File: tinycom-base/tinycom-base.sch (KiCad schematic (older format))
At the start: 9 parts, among them J1 MICRO_SD_HINGE, P1 CONN_02X08, P2 CONN_02X08, P3 USB_A, P4 CONN_01X12, P5 CONN_02X12, U1 OLIMEX_IC_AXP209, U2 STM32-48PIN, U3 fpc_24

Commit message: add base
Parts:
- removed P4: CONN_01X12, Pin_Headers:Pin_Header_Straight_1x12, symbol CONN_01X12
- removed P5: CONN_02X12, Pin_Headers:Pin_Header_Straight_2x12, symbol CONN_02X12
- removed U2: STM32-48PIN, mods:QFP50P900X900X160-48N, symbol STM32-48PIN
- removed U3: fpc_24, tinycom:fpc_24, symbol fpc_24
- added P4: USB_B, Connect:USB_Micro-B, symbol USB_B
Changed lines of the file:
@@
 LIBS:armory
 LIBS:stm32-48pin-devBoard
-LIBS:tinycom-pwm-cache
 EELAYER 25 0
 EELAYER END
@@
 $EndComp
 $Comp
-L CONN_02X12 P5
-U 1 1 562C6235
-P 4950 6400
-F 0 "P5" H 4950 7050 50  0000 C CNN
-F 1 "CONN_02X12" V 4950 6400 50  0000 C CNN
-F 2 "Pin_Headers:Pin_Header_Straight_2x12" H 4950 5200 60  0001 C CNN
-F 3 "" H 4950 5200 60  0000 C CNN
-	1    4950 6400
+L USB_B P4
+U 1 1 562CE6C3
+P 5200 6000
+F 0 "P4" H 5400 5800 50  0000 C CNN
+F 1 "USB_B" H 5150 6200 50  0000 C CNN
+F 2 "Connect:USB_Micro-B" V 5150 5900 60  0001 C CNN
+F 3 "" V 5150 5900 60  0000 C CNN
+	1    5200 6000
 	1    0    0    -1
 $EndComp
-$Comp
-L CONN_01X12 P4
-U 1 1 562C6348
-P 4450 6400
-F 0 "P4" H 4450 7050 50  0000 C CNN
-F 1 "CONN_01X12" V 4550 6400 50  0000 C CNN
-F 2 "Pin_Headers:Pin_Header_Straight_1x12" H 4450 6400 60  0001 C CNN
-F 3 "" H 4450 6400 60  0000 C CNN
-	1    4450 6400
-	1    0    0    -1
-$EndComp
-$Comp
-L STM32-48PIN U2
-U 1 1 562C67D9
-P 9350 2650
-F 0 "U2" H 8350 4400 60  0000 C CNN
-F 1 "STM32-48PIN" H 8600 850 60  0000 C CNN
-F 2 "mods:QFP50P900X900X160-48N" H 9350 2650 60  0001 C CNN
-F 3 "" H 9350 2650 60  0000 C CNN
-	1    9350 2650
-	1    0    0    -1
-$EndComp
-$Comp
-L fpc_24 U3
-U 1 1 562CDBDB
-P 9250 5050
-F 0 "U3" H 9250 5050 60  0000 C CNN
-F 1 "fpc_24" H 9250 5050 60  0000 C CNN
-F 2 "tinycom:fpc_24" H 9250 5050 60  0000 C CNN
-F 3 "" H 9250 5050 60  0000 C CNN
-	1    9250 5050
-	1    0    0    -1
-$EndComp

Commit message: xxx
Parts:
- U1: footprint ax209:ax209-OLIMEX_IC_QFN48 -> tinycom:ax209-OLIMEX_IC_QFN48
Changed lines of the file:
@@
 F 0 "U1" H 2350 6280 50  0000 L BNN
 F 1 "OLIMEX_IC_AXP209" H 2350 1250 50  0000 L BNN
-F 2 "ax209:ax209-OLIMEX_IC_QFN48" H 2850 4000 50  0001 C CNN
+F 2 "tinycom:ax209-OLIMEX_IC_QFN48" H 2850 4000 50  0001 C CNN
 F 3 "" H 2850 3850 60  0000 C CNN
 	1    2850 3850

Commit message: prepare base
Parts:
- removed U1: OLIMEX_IC_AXP209, tinycom:ax209-OLIMEX_IC_QFN48, symbol OLIMEX_IC_AXP209
- added C1, C10, C13, C2, C3, C4, C5, C6, C7, C8, C9: C_Small, Capacitors_SMD:C_0805, symbol C_Small
- added C11, C12: CP_Small, Capacitors_Elko_ThroughHole:Elko_vert_11.2x6.3mm_RM2.5_CopperClear, symbol CP_Small
- added D1: D_Schottky_Small, Diodes_SMD:SMA_Standard, symbol D_Schottky_Small
- added L1, L2, L3: SMD-INDUCTOR-2.2UH-20%-1.2A(0805), cd32:CD32, symbol SMD-INDUCTOR-2.2UH-20%-1.2A(0805)
- added R1, R10, R11, R12, R2, R3, R4, R5, R6, R7, R8, R9: R_Small, Resistors_SMD:R_0805, symbol R_Small
- added U1, U2, U3: SY8008BAAC, opendous:SOT23-5_Opendous, symbol SY8008BAAC
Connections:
- net UART1_TX: now reaches P1.1 (P1)
- net UDP1: now reaches P1.10 (P10)
- net UDP1: now also P3.3 (D+)
- net SDC0_CMD: now reaches P1.11 (P11)
- net SDC0_CMD: now also J1.3 (CMD), R10.2
- net UDM1: now reaches P1.12 (P12)
- net UDM1: now also P3.2 (D-)
- net SDC0_D3: now reaches P1.13 (P13)
- net SDC0_D3: now also J1.2 (CD/DAT3), R11.2
- net UDP0: now reaches P1.14 (P14)
- net UDP0: now also P4.3 (D+)
- net SDC0_D2: now reaches P1.15 (P15)
- net SDC0_D2: now also J1.1 (DAT2), R12.2
- net UDM0: now reaches P1.16 (P16)
- net UDM0: now also P4.2 (D-)
- net GND: now reaches P1.2 (P2)
- net GND: now also J1.10 (GND2), J1.11 (GND3), J1.12 (GND4), J1.6 (VSS), J1.9 (GND1), P2.2 (P2), P3.4 (GND), P4.4 (GND), P4.5 (shield), C1.2, C10.1, C11.2, C12.2, C13.1, C2.1, C3.2, C4.2, C5.1, C6.1, C7.1, C8.1, C9.1, R2.2, R4.2, R6.2, R7.2, U1.2 (GND), U2.2 (GND), U3.2 (GND)
- net UART1_RX: now reaches P1.3 (P3)
- net VCC_15: now reaches P1.4 (P4)
- net VCC_15: now also C5.2, L3.2, R3.1
- net SDC0_D1: now reaches P1.5 (P5)
- net SDC0_D1: now also J1.8 (DAT1), R8.2
- net VCC_14: now reaches P1.6 (P6)
- net VCC_14: now also C6.2, L2.2, R5.1
- net SDC0_D0: now reaches P1.7 (P7)
- net SDC0_D0: now also J1.7 (DAT0), R9.2
- net +3V3: now reaches P1.8 (P8)
- net +3V3: now also J1.4 (VDD), C13.2, C2.2, C8.2, D1.2 (A), L1.2, R1.1, R10.1, R11.1, R12.1, R8.1, R9.1
- net SDC0_CLK: now reaches P1.9 (P9)
- net SDC0_CLK: now also J1.5 (CLK)
- net VCC_30: now reaches P2.4 (P4)
- net VCC_30: now also C7.2, D1.1 (K), R7.1
- net +5V: now reaches P3.1 (VCC)
- net +5V: now also P4.1 (VCC), C1.1, C10.2, C11.1, C12.1, C3.1, C4.1, C9.2, U1.1 (EN), U1.4 (IN), U2.1 (EN), U2.4 (IN), U3.1 (EN), U3.4 (IN)
- new net: L1.1, U1.3 (LX)
- new net: R1.2, R2.1, U1.5 (FB)
- new net: L2.1, U2.3 (LX)
- new net: R5.2, R6.1, U2.5 (FB)
- new net: L3.1, U3.3 (LX)
- new net: R3.2, R4.1, U3.5 (FB)
- no-connect marks 0 -> 1
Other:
- moved on the sheet: J1, P1, P2, P3, P4

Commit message: adjust base
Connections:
- net GND: no longer P4.5 (shield)
- net UART1_RX: no longer names the net of P1.3 (P3)
- net UART1_TX: no longer names the net of P1.1 (P1)
- no-connect marks 1 -> 18
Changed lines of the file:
@@
 $EndComp
 $Comp
-L +5V #PWR14
+L +5V #PWR01
 U 1 1 562DA8F7
 P 5250 4200
-F 0 "#PWR14" H 5250 4050 50  0001 C CNN
+F 0 "#PWR01" H 5250 4050 50  0001 C CNN
 F 1 "+5V" H 5250 4340 50  0000 C CNN
 F 2 "" H 5250 4200 60  0000 C CNN
@@
 $EndComp
 $Comp
-L GND #PWR15
+L GND #PWR02
 U 1 1 562DA928
 P 5250 4600
-F 0 "#PWR15" H 5250 4350 50  0001 C CNN
+F 0 "#PWR02" H 5250 4350 50  0001 C CNN
 F 1 "GND" H 5250 4450 50  0000 C CNN
 F 2 "" H 5250 4600 60  0000 C CNN
@@
 UDP0
 $Comp
-L +5V #PWR16
+L +5V #PWR03
 U 1 1 562DAC42
 P 5300 5050
-F 0 "#PWR16" H 5300 4900 50  0001 C CNN
+F 0 "#PWR03" H 5300 4900 50  0001 C CNN
 F 1 "+5V" H 5300 5190 50  0000 C CNN
 F 2 "" H 5300 5050 60  0000 C CNN
@@
 $EndComp
 $Comp
-L GND #PWR17
+L GND #PWR04
 U 1 1 562DAC77
 P 5300 5500
-F 0 "#PWR17" H 5300 5250 50  0001 C CNN
+F 0 "#PWR04" H 5300 5250 50  0001 C CNN
 F 1 "GND" H 5300 5350 50  0000 C CNN
 F 2 "" H 5300 5500 60  0000 C CNN
@@
 UDP1
 $Comp
-L GND #PWR5
+L GND #PWR05
 U 1 1 562DAF0B
 P 1350 1750
-F 0 "#PWR5" H 1350 1500 50  0001 C CNN
+F 0 "#PWR05" H 1350 1500 50  0001 C CNN
 F 1 "GND" H 1350 1600 50  0000 C CNN
 F 2 "" H 1350 1750 60  0000 C CNN
@@
 $EndComp
 $Comp
-L +5V #PWR3
+L +5V #PWR06
 U 1 1 562DAF87
 P 1250 1350
-F 0 "#PWR3" H 1250 1200 50  0001 C CNN
+F 0 "#PWR06" H 1250 1200 50  0001 C CNN
 F 1 "+5V" H 1250 1490 50  0000 C CNN
 F 2 "" H 1250 1350 60  0000 C CNN
@@
 $EndComp
 $Comp
-L +5V #PWR1
+L +5V #PWR07
 U 1 1 562DB0A5
 P 1150 2550
-F 0 "#PWR1" H 1150 2400 50  0001 C CNN
+F 0 "#PWR07" H 1150 2400 50  0001 C CNN
 F 1 "+5V" H 1150 2690 50  0000 C CNN
 F 2 "" H 1150 2550 60  0000 C CNN
@@
 $EndComp
 $Comp
-L GND #PWR6
+L GND #PWR08
 U 1 1 562DB1B7
 P 1350 2900
-F 0 "#PWR6" H 1350 2650 50  0001 C CNN
+F 0 "#PWR08" H 1350 2650 50  0001 C CNN
 F 1 "GND" H 1350 2750 50  0000 C CNN
 F 2 "" H 1350 2900 60  0000 C CNN
@@
 $EndComp
 $Comp
-L +5V #PWR2
+L +5V #PWR09
 U 1 1 562DB2B7
 P 1150 3800
-F 0 "#PWR2" H 1150 3650 50  0001 C CNN
+F 0 "#PWR09" H 1150 3650 50  0001 C CNN
 F 1 "+5V" H 1150 3940 50  0000 C CNN
 F 2 "" H 1150 3800 60  0000 C CNN
@@
 $EndComp
 $Comp
-L GND #PWR4
+L GND #PWR010
 U 1 1 562DB346
 P 1300 4150
-F 0 "#PWR4" H 1300 3900 50  0001 C CNN
+F 0 "#PWR010" H 1300 3900 50  0001 C CNN
 F 1 "GND" H 1300 4000 50  0000 C CNN
 F 2 "" H 1300 4150 60  0000 C CNN
@@
 VCC_15
 $Comp
-L GND #PWR19
+L GND #PWR011
 U 1 1 562DAEC4
 P 7450 2400
-F 0 "#PWR19" H 7450 2150 50  0001 C CNN
+F 0 "#PWR011" H 7450 2150 50  0001 C CNN
 F 1 "GND" H 7450 2250 50  0000 C CNN
 F 2 "" H 7450 2400 60  0000 C CNN
@@
 	1    0    0    -1
 $EndComp
-Text GLabel 6800 2650 0    60   Input ~ 0
-UART1_RX
-Text GLabel 6800 2550 0    60   Input ~ 0
-UART1_TX
-$Comp
-L GND #PWR22
+$Comp
+L GND #PWR012
 U 1 1 562DA997
 P 8650 2450
-F 0 "#PWR22" H 8650 2200 50  0001 C CNN
+F 0 "#PWR012" H 8650 2200 50  0001 C CNN
 F 1 "GND" H 8650 2300 50  0000 C CNN
 F 2 "" H 8650 2450 60  0000 C CNN
@@
 SDC0_D1
 $Comp
-L GND #PWR20
+L GND #PWR013
 U 1 1 562DAEE9
 P 7450 4950
-F 0 "#PWR20" H 7450 4700 50  0001 C CNN
+F 0 "#PWR013" H 7450 4700 50  0001 C CNN
 F 1 "GND" H 7450 4800 50  0000 C CNN
 F 2 "" H 7450 4950 60  0000 C CNN
@@
 $EndComp
 $Comp
-L GND #PWR23
+L GND #PWR014
 U 1 1 562DAF47
 P 9050 5450
-F 0 "#PWR23" H 9050 5200 50  0001 C CNN
+F 0 "#PWR014" H 9050 5200 50  0001 C CNN
 F 1 "GND" H 9050 5300 50  0000 C CNN
 F 2 "" H 9050 5450 60  0000 C CNN
@@
 $EndComp
 $Comp
-L +3.3V #PWR18
+L +3.3V #PWR015
 U 1 1 562DB369
 P 7300 4000
-F 0 "#PWR18" H 7300 3850 50  0001 C CNN
+F 0 "#PWR015" H 7300 3850 50  0001 C CNN
 F 1 "+3.3V" H 7300 4140 50  0000 C CNN
 F 2 "" H 7300 4000 60  0000 C CNN
@@
 $EndComp
 $Comp
-L GND #PWR9
+L GND #PWR016
 U 1 1 562DB89F
 P 3250 2000
-F 0 "#PWR9" H 3250 1750 50  0001 C CNN
+F 0 "#PWR016" H 3250 1750 50  0001 C CNN
 F 1 "GND" H 3250 1850 50  0000 C CNN
 F 2 "" H 3250 2000 60  0000 C CNN
@@
 $EndComp
 $Comp
-L +3.3V #PWR10
+L +3.3V #PWR017
 U 1 1 562DBC47
 P 3600 1350
-F 0 "#PWR10" H 3600 1200 50  0001 C CNN
+F 0 "#PWR017" H 3600 1200 50  0001 C CNN
 F 1 "+3.3V" H 3600 1490 50  0000 C CNN
 F 2 "" H 3600 1350 60  0000 C CNN
@@
 $EndComp
 $Comp
-L GND #PWR8
+L GND #PWR018
 U 1 1 562F8BF0
 P 3150 3150
-F 0 "#PWR8" H 3150 2900 50  0001 C CNN
+F 0 "#PWR018" H 3150 2900 50  0001 C CNN
 F 1 "GND" H 3150 3000 50  0000 C CNN
 F 2 "" H 3150 3150 60  0000 C CNN
@@
 $EndComp
 $Comp
-L GND #PWR7
+L GND #PWR019
 U 1 1 562F9FD4
 P 3100 4550
-F 0 "#PWR7" H 3100 4300 50  0001 C CNN
+F 0 "#PWR019" H 3100 4300 50  0001 C CNN
 F 1 "GND" H 3100 4400 50  0000 C CNN
 F 2 "" H 3100 4550 60  0000 C CNN
@@
 $EndComp
 $Comp
-L GND #PWR11
+L GND #PWR020
 U 1 1 56336272
 P 4400 1900
-F 0 "#PWR11" H 4400 1650 50  0001 C CNN
+F 0 "#PWR020" H 4400 1650 50  0001 C CNN
 F 1 "GND" H 4400 1750 50  0000 C CNN
 F 2 "" H 4400 1900 60  0000 C CNN
@@
 $EndComp
 $Comp
-L +3.3V #PWR21
+L +3.3V #PWR021
 U 1 1 563494F9
 P 8050 3600
-F 0 "#PWR21" H 8050 3450 50  0001 C CNN
+F 0 "#PWR021" H 8050 3450 50  0001 C CNN
 F 1 "+3.3V" H 8050 3740 50  0000 C CNN
 F 2 "" H 8050 3600 60  0000 C CNN
@@
 $EndComp
 $Comp
-L GND #PWR12
+L GND #PWR022
 U 1 1 5634B03F
 P 4900 4550
-F 0 "#PWR12" H 4900 4300 50  0001 C CNN
+F 0 "#PWR022" H 4900 4300 50  0001 C CNN
 F 1 "GND" H 4900 4400 50  0000 C CNN
 F 2 "" H 4900 4550 60  0000 C CNN
@@
 $EndComp
 $Comp
-L GND #PWR13
+L GND #PWR023
 U 1 1 5634B0B0
 P 4900 5400
-F 0 "#PWR13" H 4900 5150 50  0001 C CNN
+F 0 "#PWR023" H 4900 5150 50  0001 C CNN
 F 1 "GND" H 4900 5250 50  0000 C CNN
 F 2 "" H 4900 5400 60  0000 C CNN
@@
 	5300 5400 5300 5500
 Wire Wire Line
-	5850 4750 5450 4750
-Wire Wire Line
-	5450 4750 5450 4550
-Wire Wire Line
 	1400 1650 1350 1650
 Wire Wire Line
@@
 	9200 5400 9200 5150
 Connection ~ 9050 5400
-Wire Wire Line
-	8900 5150 8900 5400
 Wire Wire Line
 	9000 5150 9000 5400
@@
 	7000 4650 7000 4850
 Connection ~ 7200 4850
+NoConn ~ 8400 2800
+NoConn ~ 8400 2900
+NoConn ~ 8400 3000
+NoConn ~ 8400 3100
+NoConn ~ 8400 3200
+NoConn ~ 8400 3300
+NoConn ~ 7900 2600
+NoConn ~ 7900 2700
+NoConn ~ 7900 2800
+NoConn ~ 7900 2900
+NoConn ~ 7900 3000
+NoConn ~ 7900 3100
+NoConn ~ 7900 3200
+NoConn ~ 7900 3300
+NoConn ~ 6800 2550
+NoConn ~ 6800 2650
+NoConn ~ 5850 4750
+Wire Wire Line
+	8900 5150 8900 5400
 $EndSCHEMATC

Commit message: update base board
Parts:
- P3: footprint opendous:USB-A-Receptacle-FCI_87583 -> tinycom:tc-con-usb-USB-A-H
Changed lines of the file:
@@
 F 0 "P3" H 5950 5100 50  0000 C CNN
 F 1 "USB_A" H 5700 5500 50  0000 C CNN
-F 2 "opendous:USB-A-Receptacle-FCI_87583" V 5700 5200 60  0001 C CNN
+F 2 "tinycom:tc-con-usb-USB-A-H" V 5700 5200 60  0001 C CNN
 F 3 "" V 5700 5200 60  0000 C CNN
 	1    5750 5300

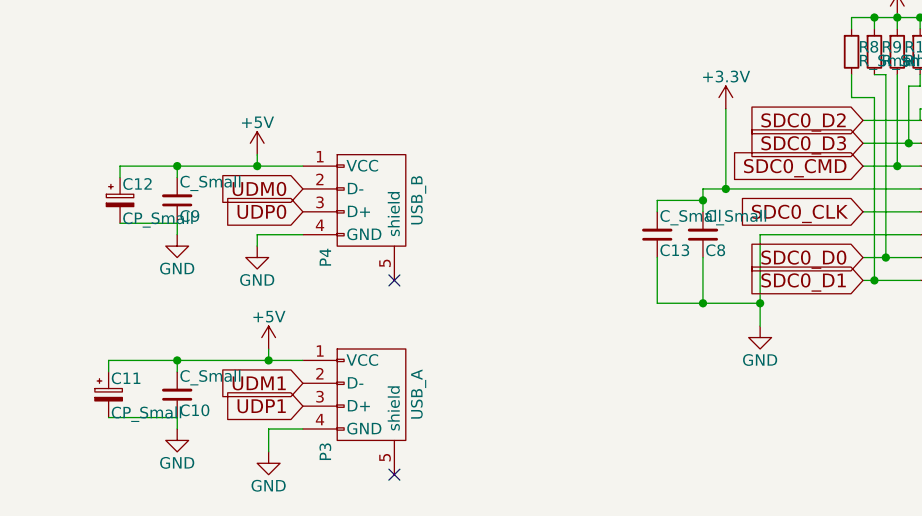
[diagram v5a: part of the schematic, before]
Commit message: route base usb+sdcard
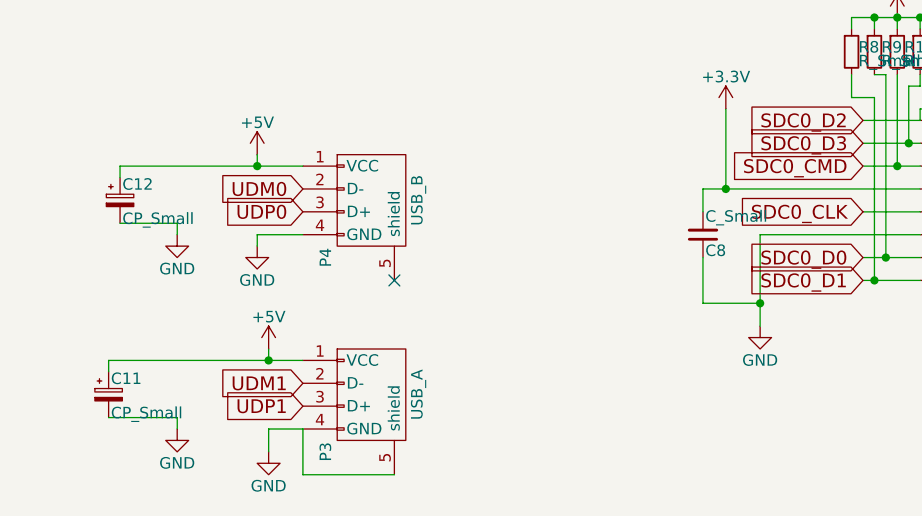
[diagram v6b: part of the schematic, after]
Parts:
- removed C10, C13, C9: C_Small, Capacitors_SMD:C_0805, symbol C_Small
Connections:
- net GND: now also P3.5 (shield)
- no-connect marks 18 -> 17
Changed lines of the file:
@@
-$EndComp
-$Comp
-L C_Small C9
-U 1 1 5634AEEE
-P 4900 4400
-F 0 "C9" H 4910 4470 50  0000 L CNN
-F 1 "C_Small" H 4910 4320 50  0000 L CNN
-F 2 "Capacitors_SMD:C_0805" H 4900 4400 60  0001 C CNN
-F 3 "" H 4900 4400 60  0000 C CNN
-	1    4900 4400
-	1    0    0    1
-$EndComp
-$Comp
-L C_Small C10
-U 1 1 5634AF93
-P 4900 5250
-F 0 "C10" H 4910 5320 50  0000 L CNN
-F 1 "C_Small" H 4910 5170 50  0000 L CNN
-F 2 "Capacitors_SMD:C_0805" H 4900 5250 60  0001 C CNN
-F 3 "" H 4900 5250 60  0000 C CNN
-	1    4900 5250
-	1    0    0    1
 $EndComp
 $Comp
@@
 Wire Wire Line
 	7200 4650 7200 4850
-Wire Wire Line
-	7000 4850 7450 4850
 Connection ~ 7450 4850
-Wire Wire Line
-	4900 5100 4900 5150
 Connection ~ 5300 5100
 Wire Wire Line
@@
 Wire Wire Line
 	4900 4500 4900 4550
-Wire Wire Line
-	4900 4300 4900 4250
 Connection ~ 5250 4250
 Wire Wire Line
 	4650 4250 4650 4300
-Connection ~ 4900 4250
 Wire Wire Line
 	4650 4500 4900 4500
@@
 Wire Wire Line
 	4600 5100 4600 5150
-Connection ~ 4900 5100
 Wire Wire Line
 	4600 5350 4900 5350
@@
 	1    0    0    -1
 $EndComp
-NoConn ~ 5850 5600
-$Comp
-L C_Small C13
-U 1 1 5634DEA7
-P 7000 4550
-F 0 "C13" H 7010 4620 50  0000 L CNN
-F 1 "C_Small" H 7010 4470 50  0000 L CNN
-F 2 "Capacitors_SMD:C_0805" H 7000 4550 60  0001 C CNN
-F 3 "" H 7000 4550 60  0000 C CNN
-	1    7000 4550
-	1    0    0    1
-$EndComp
-Wire Wire Line
-	7200 4400 7000 4400
-Wire Wire Line
-	7000 4400 7000 4450
-Connection ~ 7200 4400
-Wire Wire Line
-	7000 4650 7000 4850
-Connection ~ 7200 4850
 NoConn ~ 8400 2800
 NoConn ~ 8400 2900
@@
 Wire Wire Line
 	8900 5150 8900 5400
+Wire Wire Line
+	5850 5600 5450 5600
+Wire Wire Line
+	5450 5600 5450 5400
+Wire Wire Line
+	7200 4850 7450 4850
 $EndSCHEMATC

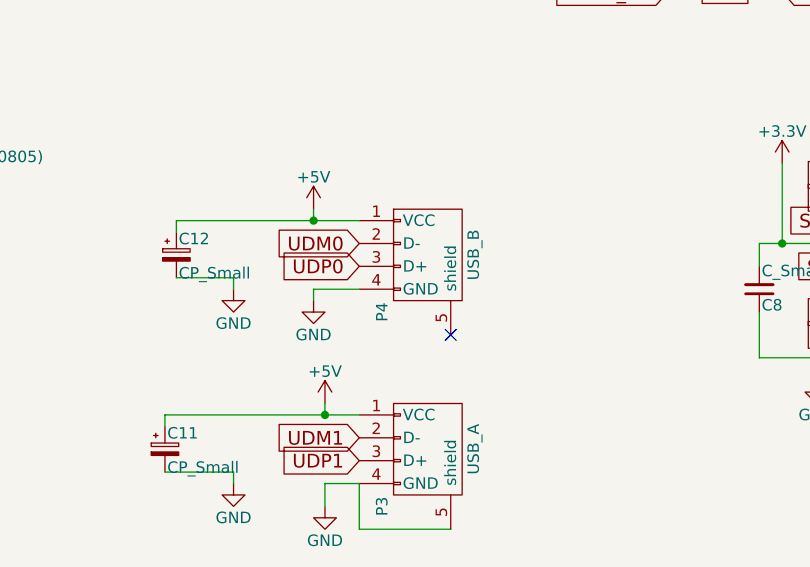
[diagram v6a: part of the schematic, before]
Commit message: add uboot_sel test point
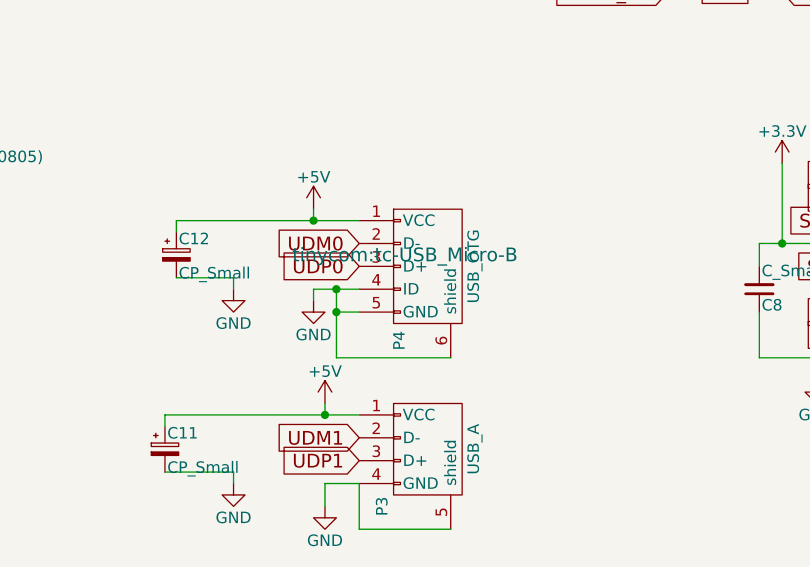
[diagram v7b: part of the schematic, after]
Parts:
- removed P4: USB_B, Connect:USB_Micro-B, symbol USB_B
- added P4: USB_OTG, tinycom:tc-USB_Micro-B, symbol USB_OTG
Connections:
- net +5V: now also P4.1 (VCC)
- net GND: now also P4.4 (ID), P4.5 (GND), P4.6 (shield)
- net UDM0: now also P4.2 (D-)
- net UDP0: now also P4.3 (D+)
- no-connect marks 17 -> 16

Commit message: improve base board
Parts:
- removed C1, C3, C4: C_Small, Capacitors_SMD:C_0805, symbol C_Small
- removed P1, P2: CONN_02X08, Socket_Strips:Socket_Strip_Straight_2x08, symbol CONN_02X08
- removed R10, R11, R12, R8, R9: R_Small, Resistors_SMD:R_0805, symbol R_Small
- added P1, P2: CONN_02X10, Socket_Strips:Socket_Strip_Straight_2x10, symbol CONN_02X10
- added U4: RTL8188, tinycom:RTL8188, symbol RTL8188
- added U5: rainsun-antenna, tinycom:rainsun-antenna, symbol rainsun-antenna
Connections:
- net labels added: HCEC, HCSL, HHPD, HPCOM, HPL, HPR, HSDA, HTX0N, HTX0P, HTX1N, HTX1P, HTX2N, HTX2P, HTXCN, HTXCP, MICIN1, SATA_RXM, SATA_RXP, SATA_TXM, SATA_TXP, UART0_RX, UART0_TX, UD0_N, UD0_P, UD1_N, UD1_P, UD2_N, UD2_P, VCC_12
- net labels removed: UDM0, UDM1, UDP0, UDP1, VCC_14
- wire segments 124 -> 117
- no-connect marks 16 -> 0
